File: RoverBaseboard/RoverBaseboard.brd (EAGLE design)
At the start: 87 x 61.6 mm, 60 parts, among them IC1 7805, IC3 3.3V, U2 microSD

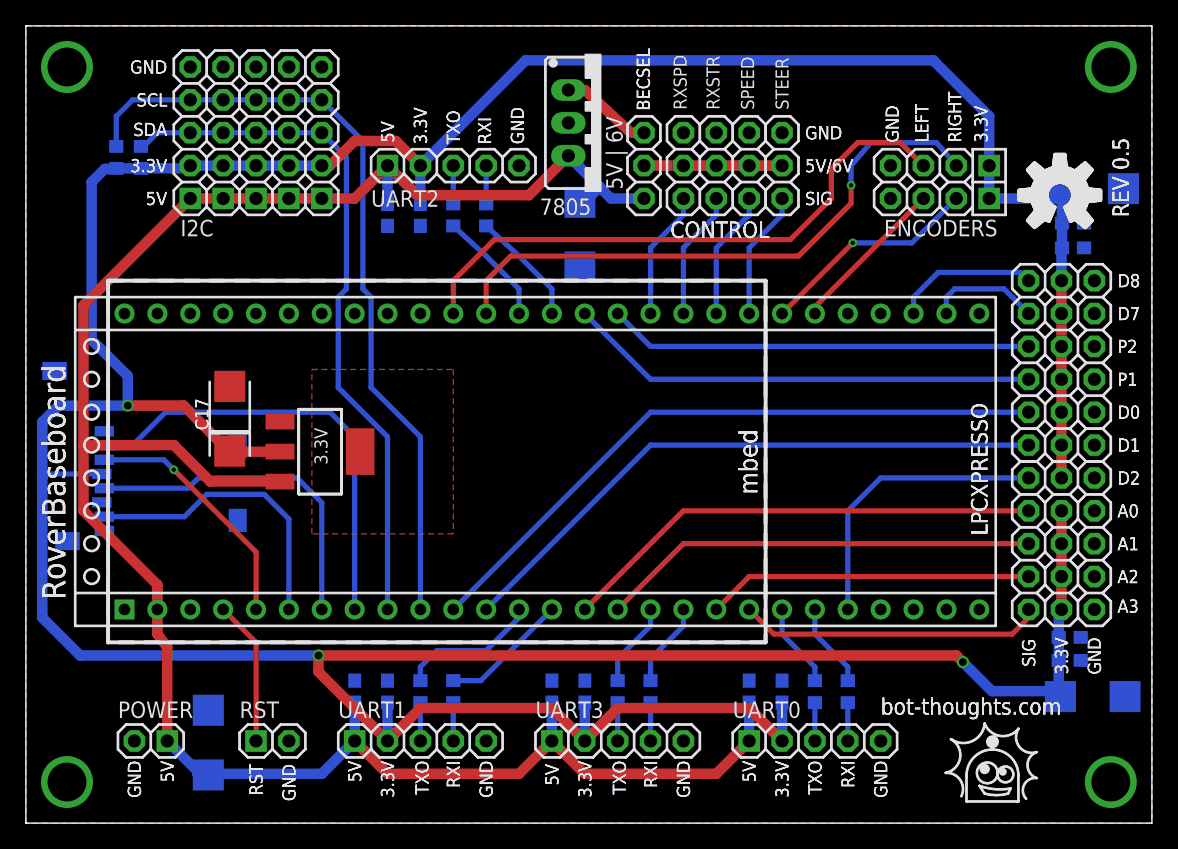
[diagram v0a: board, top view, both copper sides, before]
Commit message: Revised power hookup; 3.3V to 3.3V pin, disconnect EXT_POWER from 5V.
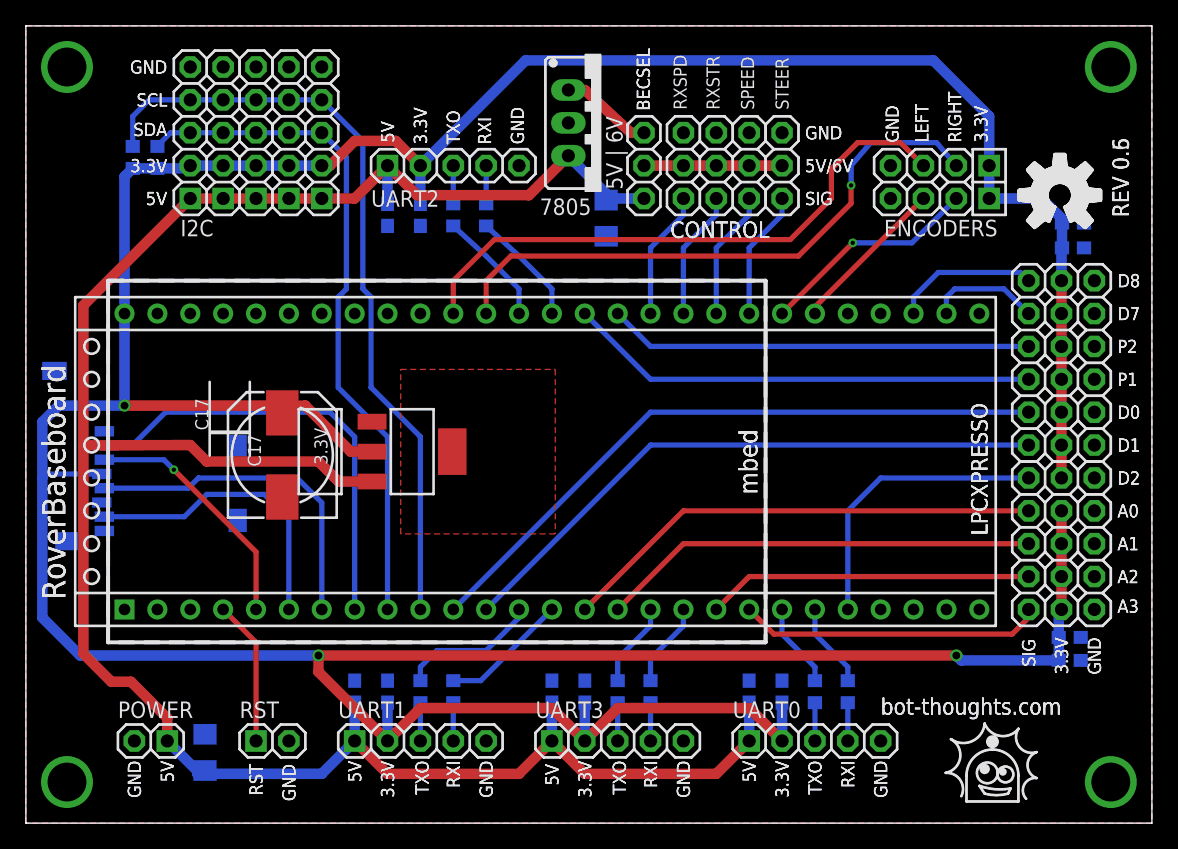
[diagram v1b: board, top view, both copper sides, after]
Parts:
- removed C1, C16: 470, bt_rcl:SMC_C
- C17: value 470 -> 100; device bt_rcl:SMC_C -> rcl:140CLH-0810
- C2, C3: value 470 -> 10; device bt_rcl:SMC_C -> rcl:C1206
- R1, R10, R2, R3, R4, R7, R8, R9: value 220 -> 10K
- moved IC3 7.11 mm to (29.8, 28.7)
- moved C17 4.93 mm to (19.8, 28.4)
- moved C3 2.40 mm to (44.8, 46.7)
- moved R6 1.27 mm to (8.26, 51.4)
- moved R5 1.27 mm to (10.2, 51.4)
- moved C2 0.80 mm to (13.8, 5.46)
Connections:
- net +3V3: now also U$1.J6-28; no longer C1.+, C16.+
- net +5V: now also C2.1, C3.1; no longer C2.+, C3.+, U$1.J6-2
- net GND: now also C2.2, C3.2; no longer C1.-, C16.-, C2.-, C3.-
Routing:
- net +5V: track 171.0 -> 176.9 mm
- net +3V3: track 320.7 -> 319.2 mm
- net SCL: track 61.3 -> 60.0 mm
- net SDA: track 53.9 -> 52.7 mm
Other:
- board text added: "REV 0.6"
